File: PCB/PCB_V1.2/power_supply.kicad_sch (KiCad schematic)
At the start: 20 parts, among them IC1 NIS4461MT3TXG, IC2 MC34063ADR2G, J10 KH-DC-050-2.0STM

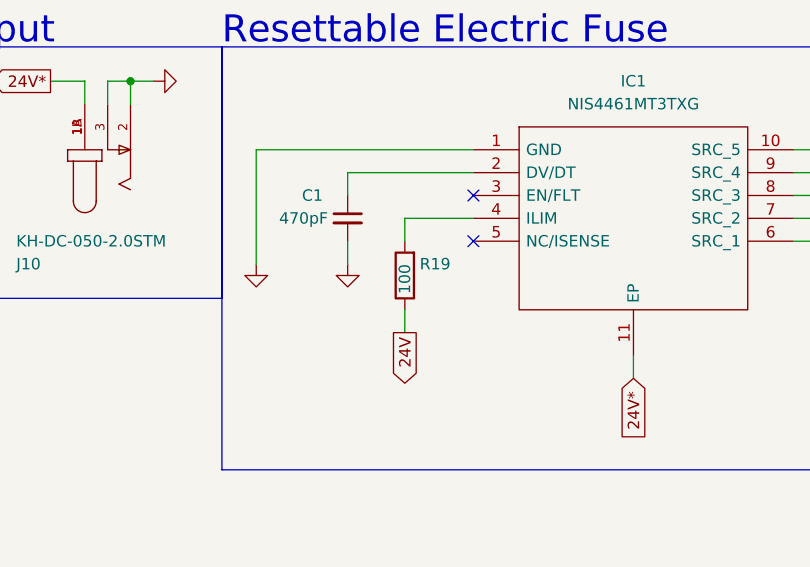
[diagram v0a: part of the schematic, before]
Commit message: PCB: added power sensor
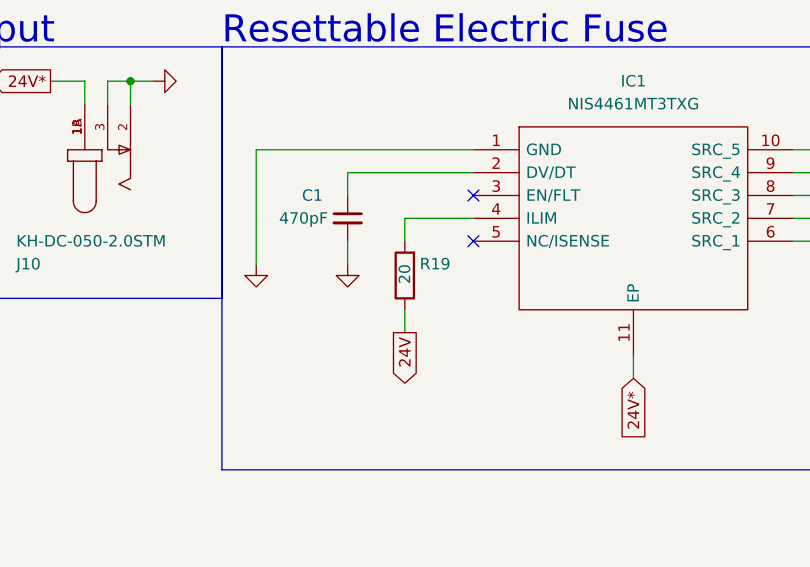
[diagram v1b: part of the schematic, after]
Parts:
- R19: value 100 -> 20
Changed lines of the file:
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@@
       (effects (font (size 1.27 1.27)) (justify left))
     )
-    (property "Value" "100" (id 1) (at 82.55 88.9 90)
+    (property "Value" "20" (id 1) (at 82.55 88.9 90)
       (effects (font (size 1.27 1.27)) (justify left))
     )
